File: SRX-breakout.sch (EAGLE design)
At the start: 9 parts

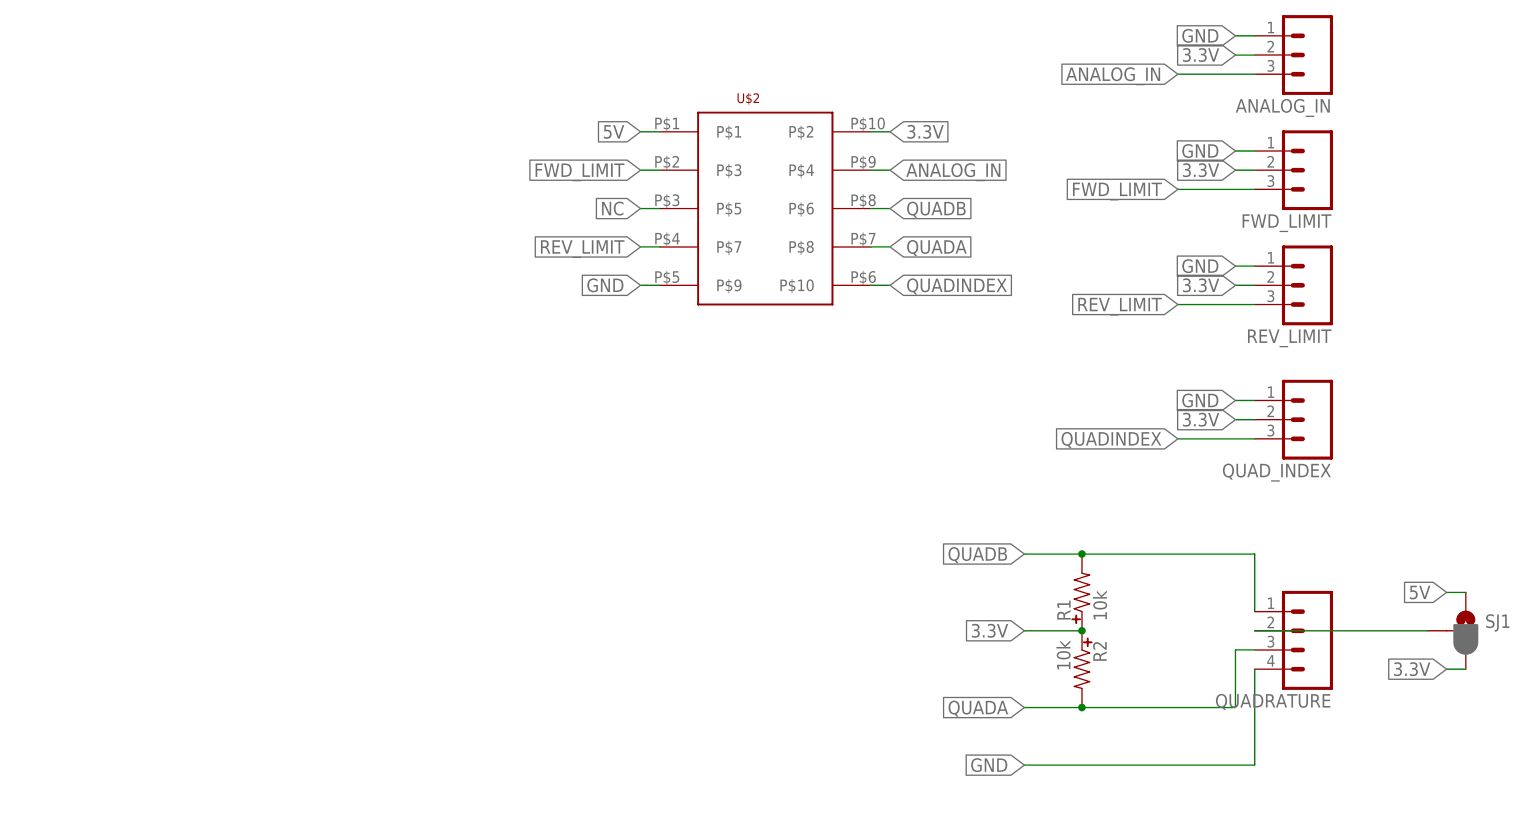
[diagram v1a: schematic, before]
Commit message: Add CAN subboard
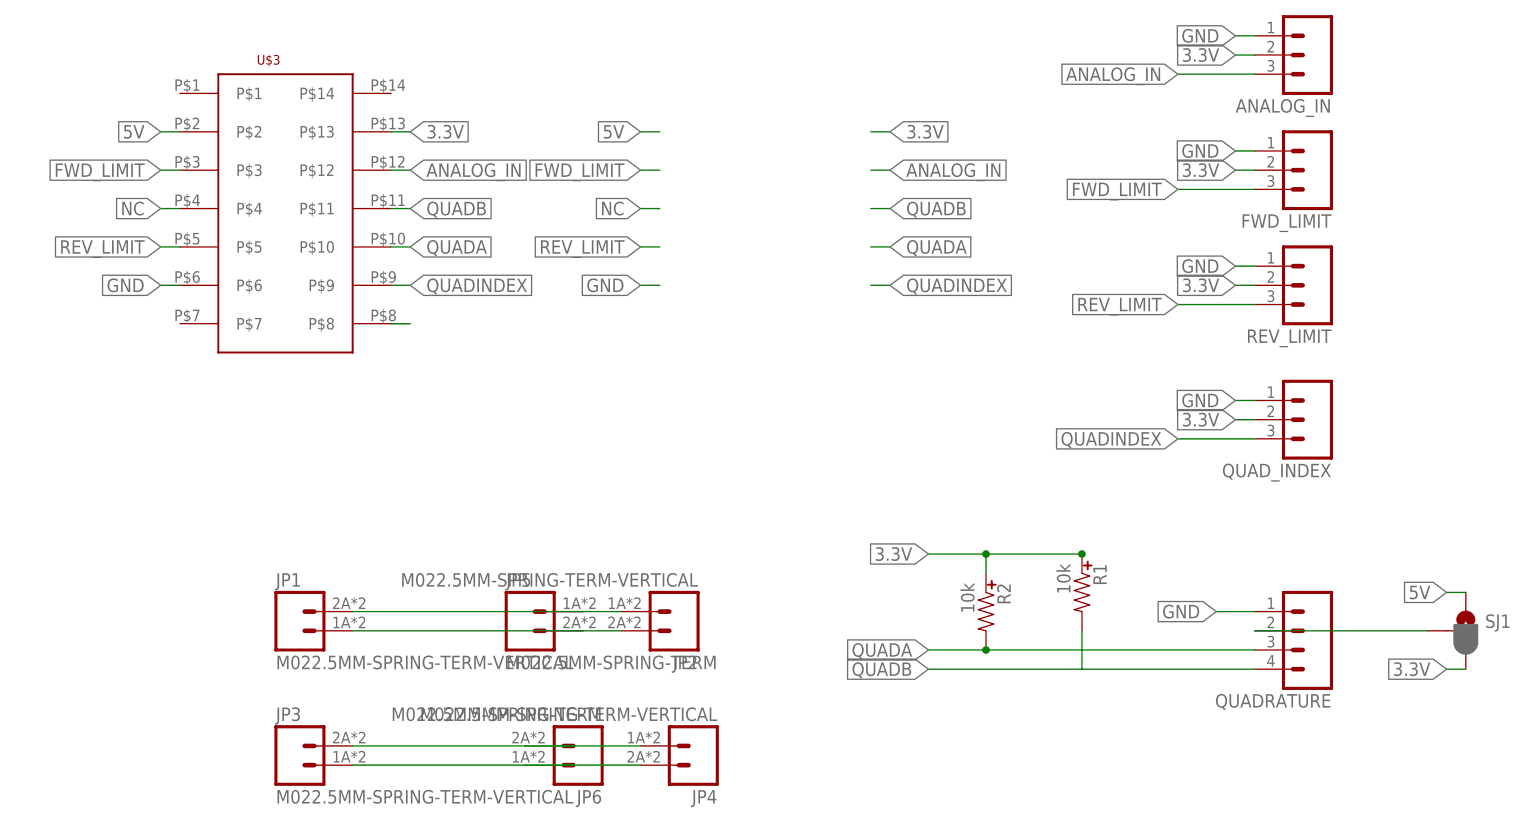
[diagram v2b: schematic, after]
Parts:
- removed U$2: M05X0250MIL, tekdemo:M05X0250MIL
- added JP1, JP2, JP3, JP4: M022.5MM-SPRING-TERM-VERTICAL, tekdemo:M022.5MM-SPRING-TERM-VERTICAL
- added JP5, JP6: M022.5MM-SPRING-TERM, tekdemo:M022.5MM-SPRING-TERM
- added U$3: M07X0220021321-00014TFLF, tekdemo:M07X0220021321-00014TFLF
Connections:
- net N$1 renamed QUAD_VOLTAGE
- new net N$1: JP3.2, JP4.1, JP6.1
- new net N$6: JP3.1, JP4.2, JP6.2
- new net N$7: JP1.1, JP2.2, JP5.1
- new net N$8: JP1.2, JP2.1, JP5.2
- net 3.3V: now also U$3.P$13; no longer U$2.P$2
- net 5V: now also U$3.P$2; no longer U$2.P$1
- net ANALOG_IN: now also U$3.P$12; no longer U$2.P$4
- net FWD_LIMIT: now also U$3.P$3; no longer U$2.P$3
- net GND: now also QUADRATURE.1, U$3.P$6; no longer QUADRATURE.4, U$2.P$9
- net NC: now also U$3.P$4; no longer U$2.P$5
- net QUADA: now also U$3.P$10; no longer U$2.P$8
- net QUADB: now also QUADRATURE.4, U$3.P$11; no longer QUADRATURE.1, U$2.P$6
- net QUADINDEX: now also U$3.P$9; no longer U$2.P$10
- net REV_LIMIT: now also U$3.P$5; no longer U$2.P$7
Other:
- moved on the sheet: R1, R2
